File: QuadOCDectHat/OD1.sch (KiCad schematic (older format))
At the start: 5 parts, among them IC1 MCT6H, T1 In Track Out

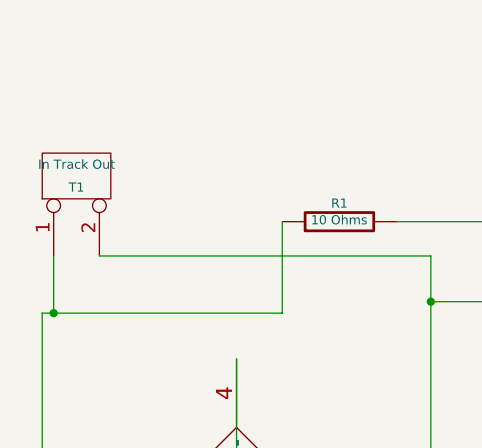
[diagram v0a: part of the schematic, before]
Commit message: Tweak PCB Silk Screen for QuadOCDetHat.
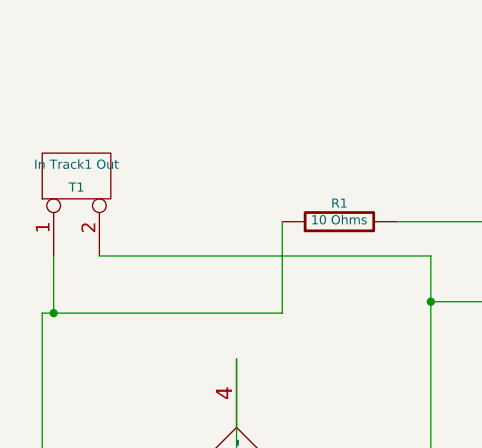
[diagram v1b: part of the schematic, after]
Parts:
- T1: value In Track Out -> In Track1 Out
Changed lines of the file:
@@
 $Descr A4 11693 8268
 encoding utf-8
-Sheet 3 5
+Sheet 2 5
 Title ""
-Date "23 feb 2019"
+Date "24 feb 2019"
 Rev ""
 Comp ""
@@
 AR Path="/5C70AEE5/5C70A943" Ref="T1"  Part="1"
 F 0 "T1" V 1300 1300 40  0000 C CNN
-F 1 "In Track Out" V 1400 1300 40  0000 C CNN
+F 1 "In Track1 Out" V 1400 1300 40  0000 C CNN
 F 2 "~" H 1350 1300 60  0000 C CNN
 F 3 "~" H 1350 1300 60  0000 C CNN

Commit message: Add Part numbers for OC HAT
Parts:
- D1: Mouser Part Number (none) -> 750-KBL401-G
- IC1: Mouser Part Number (none) -> 782-MCT6H
- R1: Mouser Part Number (none) -> CFR-25JR-52-10R
- R2: Mouser Part Number (none) -> 603-CFR-25JB-52-10K
- T1: Mouser Part Number (none) -> 649-220316-H021B01LF
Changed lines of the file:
@@
 Sheet 2 5
 Title ""
-Date "24 feb 2019"
+Date "2 jun 2019"
 Rev ""
 Comp ""
@@
 F 2 "~" H 1350 1300 60  0000 C CNN
 F 3 "~" H 1350 1300 60  0000 C CNN
+F 4 "649-220316-H021B01LF" H 1350 1300 60  0001 C CNN "Mouser Part Number"
 	1    1350 1300
 	0    -1   -1   0
@@
 F 2 "~" V 2430 1500 30  0000 C CNN
 F 3 "~" H 2500 1500 30  0000 C CNN
+F 4 "CFR-25JR-52-10R" H 2500 1500 60  0001 C CNN "Mouser Part Number"
 	1    2500 1500
 	0    -1   -1   0
@@
 F 2 "DIP-8__300" H 3540 1420 30  0001 C CIN
 F 3 "~" H 3700 1600 60  0000 C CNN
+F 4 "782-MCT6H " H 3700 1600 60  0001 C CNN "Mouser Part Number"
 	1    3700 1600
 	1    0    0    -1
@@
 F 2 "DIP-8__300" H 3540 1970 30  0001 C CIN
 F 3 "~" H 3700 2150 60  0000 C CNN
+F 4 "782-MCT6H " H 3700 2150 60  0001 C CNN "Mouser Part Number"
 	2    3700 2150
 	1    0    0    -1
@@
 F 2 "~" V 4230 1100 30  0000 C CNN
 F 3 "~" H 4300 1100 30  0000 C CNN
+F 4 "603-CFR-25JB-52-10K" H 4300 1100 60  0001 C CNN "Mouser Part Number"
 	1    4300 1100
 	1    0    0    -1
@@
 F 2 "~" H 2050 2950 60  0000 C CNN
 F 3 "~" H 2050 2950 60  0000 C CNN
+F 4 "750-KBL401-G" H 2050 2950 60  0001 C CNN "Mouser Part Number"
 	1    2050 2950
 	0    1    1    0

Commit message: QuadOCDectHat updates
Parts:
- R1, R2: symbol R -> R-RESCUE-QuadOCDectHat
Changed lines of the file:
@@
 EESchema Schematic File Version 2
+LIBS:QuadOCDectHat-rescue
 LIBS:power
 LIBS:device
@@
 LIBS:memory
 LIBS:xilinx
-LIBS:special
 LIBS:microcontrollers
 LIBS:dsp
@@
 LIBS:bridge
 LIBS:QuadOCDectHat-cache
-EELAYER 27 0
+EELAYER 25 0
 EELAYER END
 $Descr A4 11693 8268
@@
 $EndComp
 $Comp
-L R R1
+L R-RESCUE-QuadOCDectHat R1
 U 1 1 5C70A952
 P 2500 1500
@@
 $EndComp
 $Comp
-L R R2
+L R-RESCUE-QuadOCDectHat R2
 U 1 1 5C70A98C
 P 4300 1100
@@
 Connection ~ 4300 1500
 $Comp
-L +3.3V #PWR03
+L +3.3V-RESCUE-QuadOCDectHat #PWR03
 U 1 1 5C70AC29
 P 4300 750
 AR Path="/5C70A8FB/5C70AC29" Ref="#PWR03"  Part="1"
 AR Path="/5C70AEE5/5C70AC29" Ref="#PWR?"  Part="1"
+AR Path="/5C70AC29" Ref="#PWR03"  Part="1"
 F 0 "#PWR03" H 4300 710 30  0001 C CNN
 F 1 "+3.3V" H 4300 860 30  0000 C CNN
@@
 	4300 750  4300 850
 $Comp
-L GND #PWR04
+L GND-RESCUE-QuadOCDectHat #PWR04
 U 1 1 5C70AC50
 P 4200 2450
